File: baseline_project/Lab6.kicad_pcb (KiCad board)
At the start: 2 copper layers, 115 x 94 mm, 5 parts, among them IC1 TM4C123GH6PMIR, SW101 UP, U1 Adafruit ST7735R

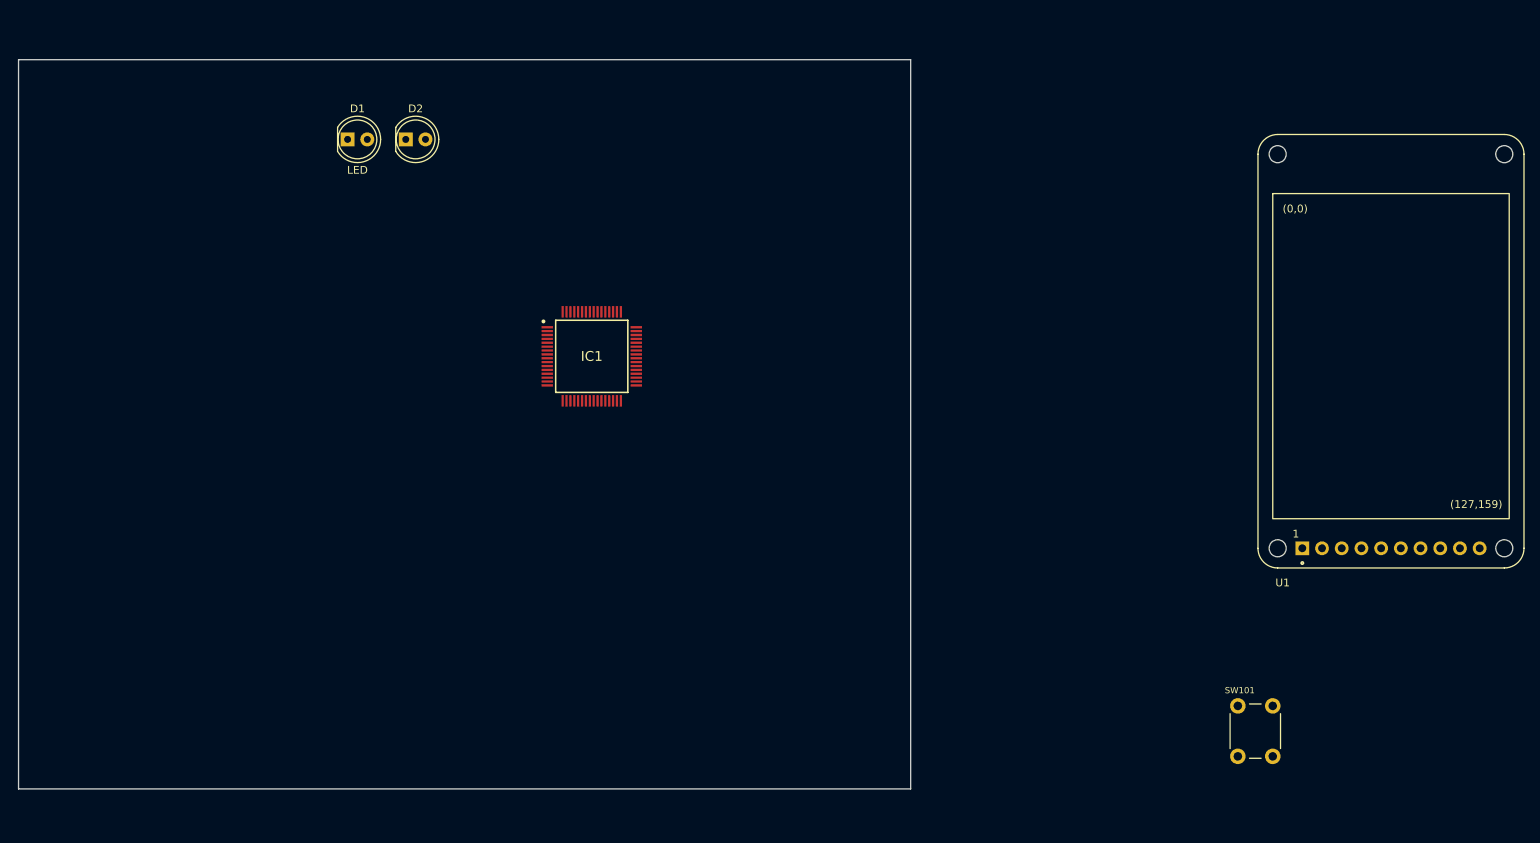
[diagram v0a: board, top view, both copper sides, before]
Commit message: Lab6 starter version 2
Needs some starter PCB place and trace
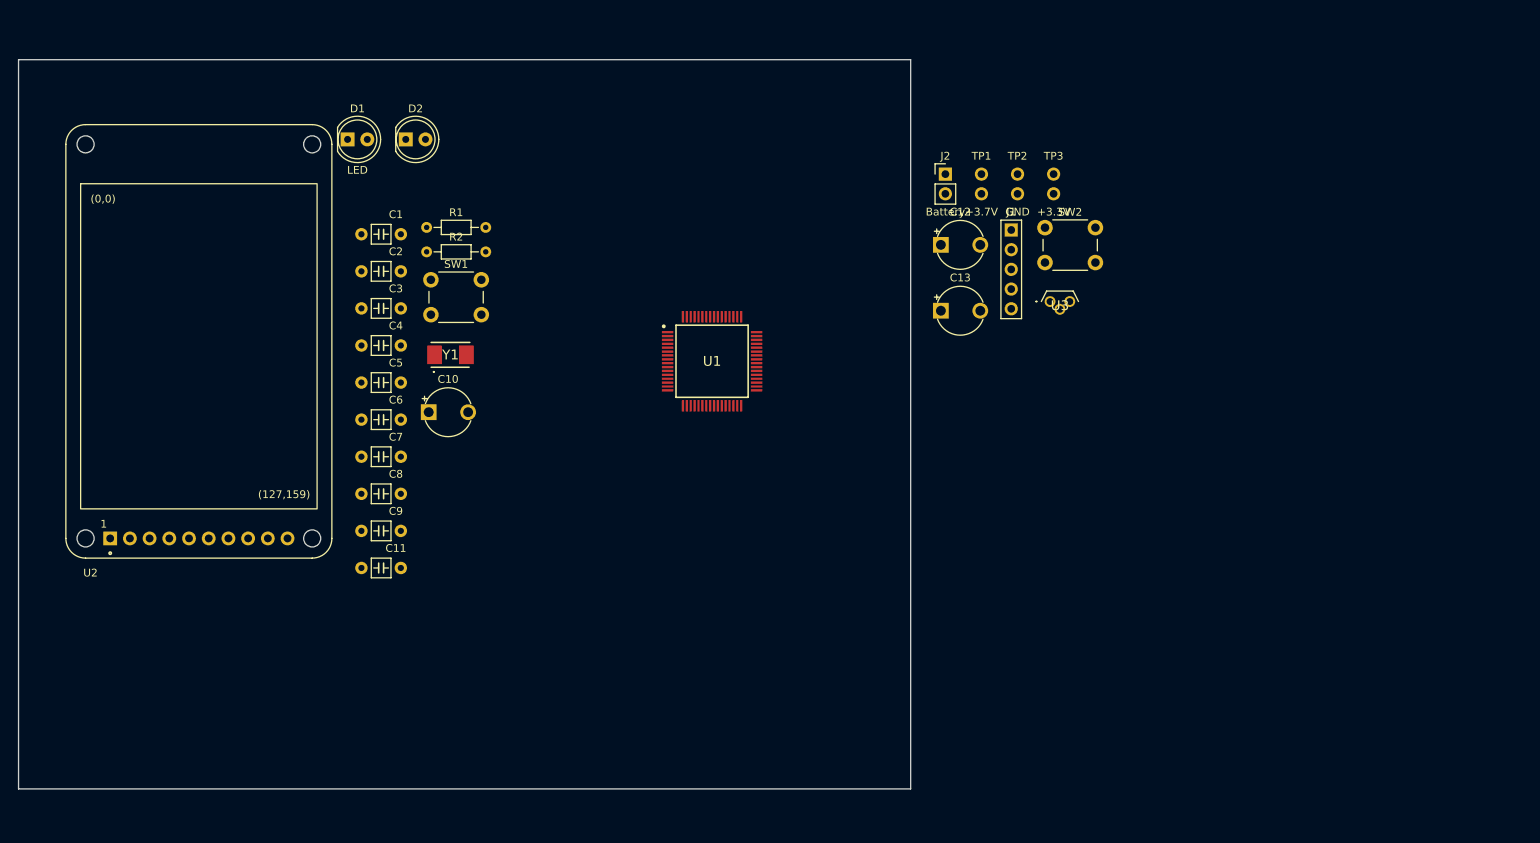
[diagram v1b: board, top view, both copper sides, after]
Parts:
- removed IC1: TM4C123GH6PMIR, ECE445L:QFP50P1200X1200X160-64N
- removed SW101: UP, Button_Switch_THT:SW_PUSH_6mm
- added C1: 10pF C0G, ECE445L:C_Axial_200mil, F.Cu at (76.2, 53.5)
- added C10: 2.2uF, ECE445L:CP_Radial_Tantal200mil, F.Cu at (84.9, 76.4)
- added C11: 0.01uF, ECE445L:C_Axial_200mil, F.Cu at (76.2, 96.5)
- added C12: 4.7uF, ECE445L:CP_Radial_Tantal200mil, F.Cu at (150.9, 54.9)
- added C13: 4.7uF, ECE445L:CP_Radial_Tantal200mil, F.Cu at (150.9, 63.4)
- added C2: 10pF C0G, ECE445L:C_Axial_200mil, F.Cu at (76.2, 58.3)
- added C3: 1uF, ECE445L:C_Axial_200mil, F.Cu at (76.2, 63.1)
- added C4: 0.1uF, ECE445L:C_Axial_200mil, F.Cu at (76.2, 67.8)
- added C5: 0.01uF, ECE445L:C_Axial_200mil, F.Cu at (76.2, 72.6)
- added C6: 0.1uF, ECE445L:C_Axial_200mil, F.Cu at (76.2, 77.4)
- added C7: 0.1uF, ECE445L:C_Axial_200mil, F.Cu at (76.2, 82.2)
- added C8: 0.1uF, ECE445L:C_Axial_200mil, F.Cu at (76.2, 87.0)
- added C9: 1uF, ECE445L:C_Axial_200mil, F.Cu at (76.2, 91.7)
- added J1: JTAG, ECE445L:PinHeader_1x05_P2.54mm_Vertical, F.Cu at (160.0, 53.0)
- added J2: Battery, ECE445L:PinHeader_1x02_P2.54mm_Vertical, F.Cu at (151.5, 45.8)
- added R1: 1M, ECE445L:R_Axial_DIN0204_L3.6mm_D1.6mm_P7.62mm_Horizontal, F.Cu at (84.6, 52.6)
- added R2: 10k, ECE445L:R_Axial_DIN0204_L3.6mm_D1.6mm_P7.62mm_Horizontal, F.Cu at (84.6, 55.8)
- added SW1: Reset, Button_Switch_THT:SW_PUSH_6mm, F.Cu at (85.2, 59.4)
- added SW2: Input, Button_Switch_THT:SW_PUSH_6mm, F.Cu at (164.3, 52.6)
- added TP1: +3.7V, ECE445L:Testpoint_1x02_P2.54mm, F.Cu at (156.1, 45.8)
- added TP2: GND, ECE445L:Testpoint_1x02_P2.54mm, F.Cu at (160.8, 45.8)
- added TP3: +3.3V, ECE445L:Testpoint_1x02_P2.54mm, F.Cu at (165.4, 45.8)
- added U2: Adafruit ST7735R, ECE445L:adafruit_st7735r2, F.Cu at (55.2, 67.3)
- added U3: LP2950-33LPRE3, ECE445L:TL431CLPM, F.Cu at (165.0, 62.2)
- added Y1: ABM3-16.000MHZ-B2-T, ECE445L:ABM3, F.Cu at (87.7, 69.0)
- U1: value Adafruit ST7735R -> TM4C123GH6PMIR; footprint ECE445L:adafruit_st7735r2 -> ECE445L:QFP50P1200X1200X160-64N
- moved U1 87.5 mm to (121.4, 69.9)
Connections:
- U1 pad 1: unconnected-(U1-GND-Pad1) -> PB6
- U1 pad 10: unconnected-(U1-LITE-Pad10) -> PD7
- U1 pad 2: unconnected-(U1-VCC-Pad2) -> +3V3
- U1 pad 3: unconnected-(U1-RESET-Pad3) -> GND
- U1 pad 4: unconnected-(U1-D/C-Pad4) -> PB7
- U1 pad 5: unconnected-(U1-CARD_CS-Pad5) -> PF4
- U1 pad 6: unconnected-(U1-TFT_CS-Pad6) -> PE3
- U1 pad 7: unconnected-(U1-MOSI-Pad7) -> PE2
- U1 pad 8: unconnected-(U1-SCK-Pad8) -> PE1
- U1 pad 9: unconnected-(U1-MISO-Pad9) -> PE0

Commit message: Lab6 starter
I am ready to release Lab6 starter and updated ECE445L library
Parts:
- added H1: ~, ECE445L:MountingHole_4_40, F.Cu at (35.6, 29.2)
- added H2: ~, ECE445L:MountingHole_4_40, F.Cu at (142.2, 29.2)
- added H3: ~, ECE445L:MountingHole_4_40, F.Cu at (142.2, 110.5)
- added H4: ~, ECE445L:MountingHole_4_40, F.Cu at (35.6, 110.5)
- moved U2 121.7 mm to (172.7, 99.1)
- moved D1 91.5 mm to (165.7, 34.9)
- moved D2 72.6 mm to (154.3, 35.6)
- moved R2 62.7 mm to (144.1, 75.6), turned to -90 degrees
- moved C1 58.2 mm to (132.7, 67.3)
- moved C2 58.0 mm to (132.7, 71.2)
- moved SW1 57.9 mm to (139.8, 78.7), turned to -90 degrees
- moved R1 53.9 mm to (125.1, 88.3), turned to 90 degrees
- moved C3 52.7 mm to (128.9, 61.7)
- moved C7 50.0 mm to (117.5, 54.0), turned to 90 degrees
- moved C8 49.0 mm to (112.4, 54.0), turned to 90 degrees
- moved C5 44.7 mm to (120.0, 81.3), turned to -90 degrees
- moved Y1 41.1 mm to (128.8, 69.2), turned to 90 degrees
- moved C4 41.0 mm to (114.9, 81.3), turned to -90 degrees
- moved C11 40.3 mm to (101.0, 64.8), turned to 180 degrees
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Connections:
- C5 pad 1: Net-(U1-VDD_2) -> +3V3
- U1 pad 26: Net-(U1-VDD_2) -> +3V3
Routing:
- net +3V3: track 0.00 -> 49.9 mm
- net /LDO: track 0.00 -> 27.8 mm
- net /OSC2: track 0.00 -> 12.5 mm
- net /OSC1: track 0.00 -> 12.2 mm
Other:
- board size 115 x 94 mm -> 114.4 x 88.9 mm

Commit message: added PD6
fixed ERC error with two +3V3 nets
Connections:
- U1 pad 53: unconnected-(U1-PD6-Pad53) -> PD6
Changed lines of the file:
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@@
   (net 8 "unconnected-(U1-~{HIB}-Pad33)")
   (net 9 "unconnected-(U1-XOSC1-Pad36)")
-  (net 10 "unconnected-(U1-PD6-Pad53)")
+  (net 10 "PD6")
   (net 11 "unconnected-(U2-GND-Pad1)")
   (net 12 "unconnected-(U2-VCC-Pad2)")
@@
       (net 22 "/TCK") (pinfunction "PC0/TCK/SWCLK") (pintype "passive"))
     (pad "53" smd rect (at 1.75 -5.738) (size 0.3 1.475) (layers "F.Cu" "F.Paste" "F.Mask")
-      (net 10 "unconnected-(U1-PD6-Pad53)") (pinfunction "PD6") (pintype "passive"))
+      (net 10 "PD6") (pinfunction "PD6") (pintype "passive"))
     (pad "54" smd rect (at 1.25 -5.738) (size 0.3 1.475) (layers "F.Cu" "F.Paste" "F.Mask")
       (net 4 "+3V3") (pinfunction "VDD_4") (pintype "passive"))
